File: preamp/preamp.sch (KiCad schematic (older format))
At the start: 37 parts, among them P1 Plug entrada, U1 N35532, U2 N35532

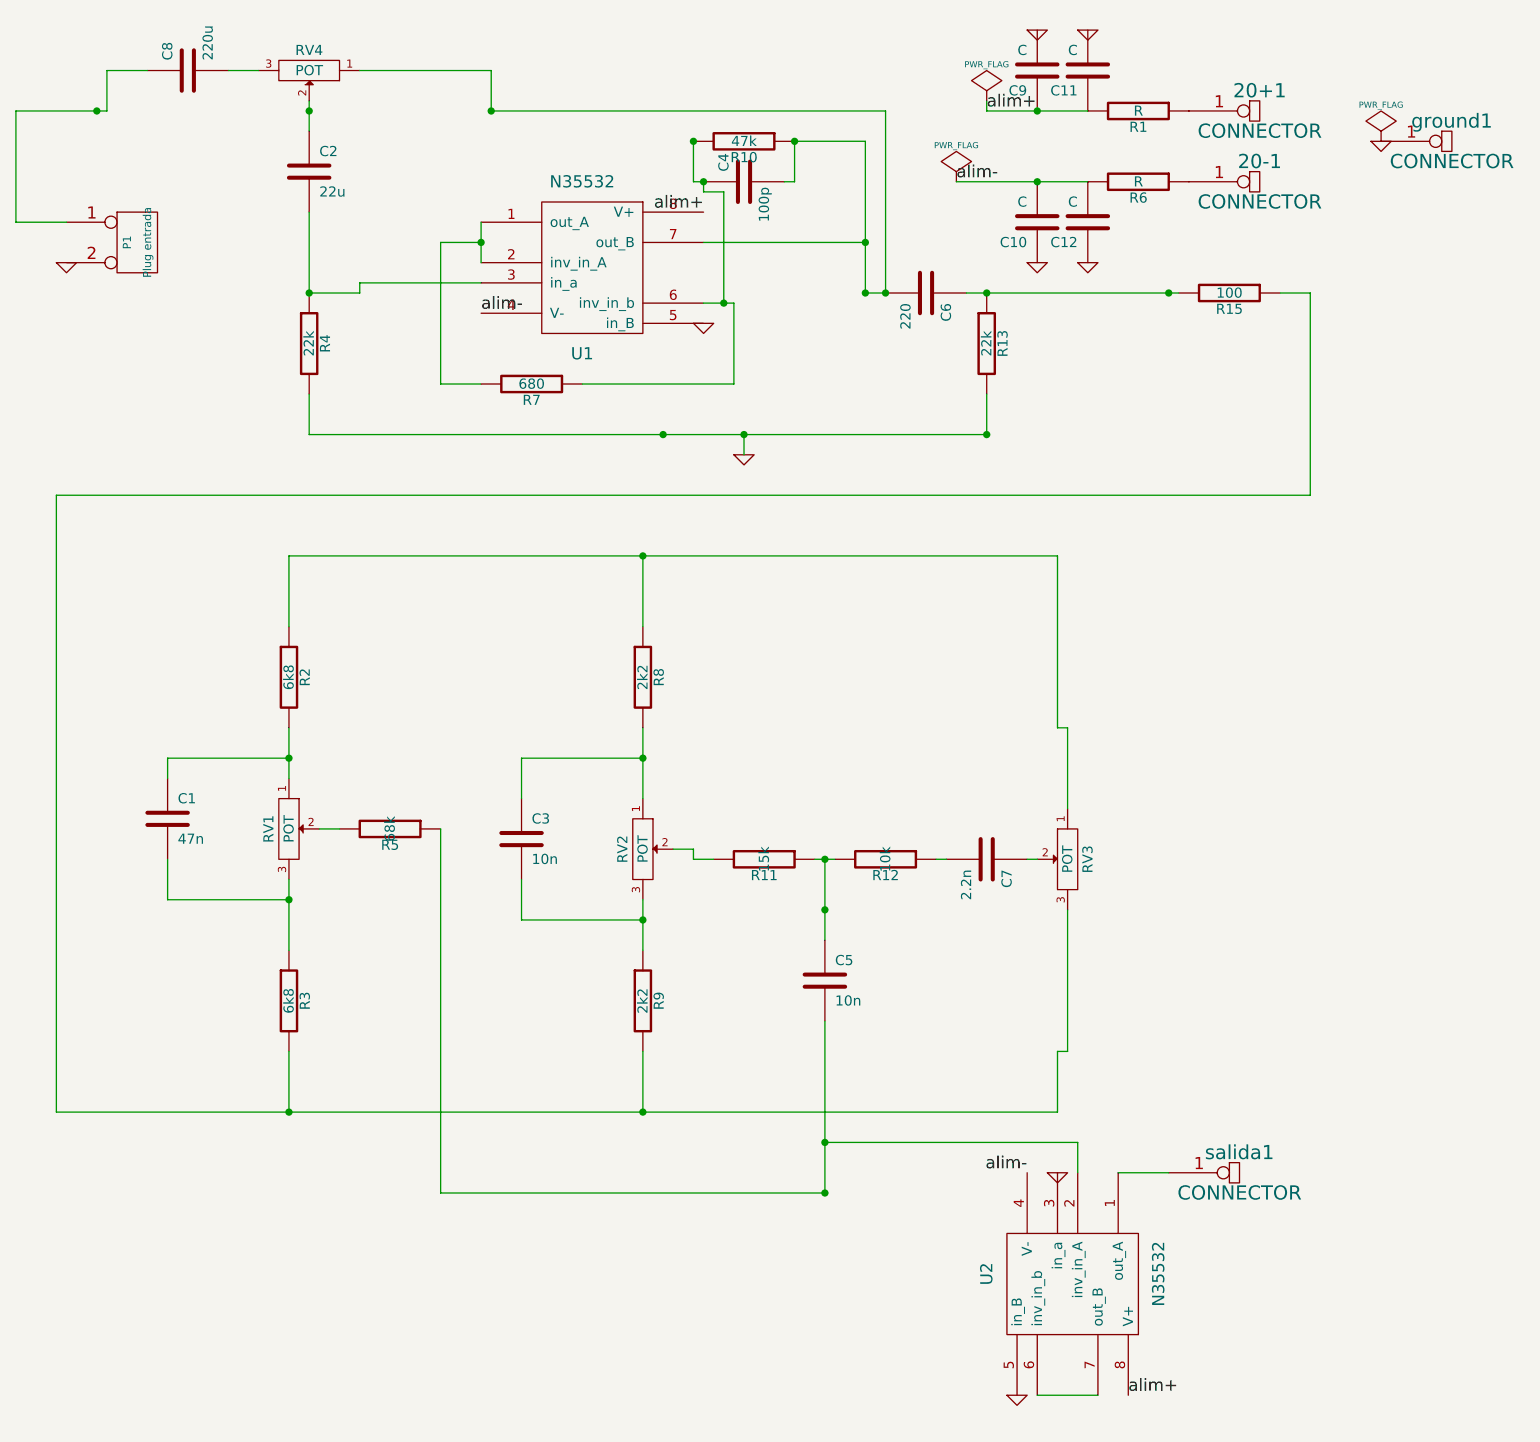
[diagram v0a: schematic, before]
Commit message: 
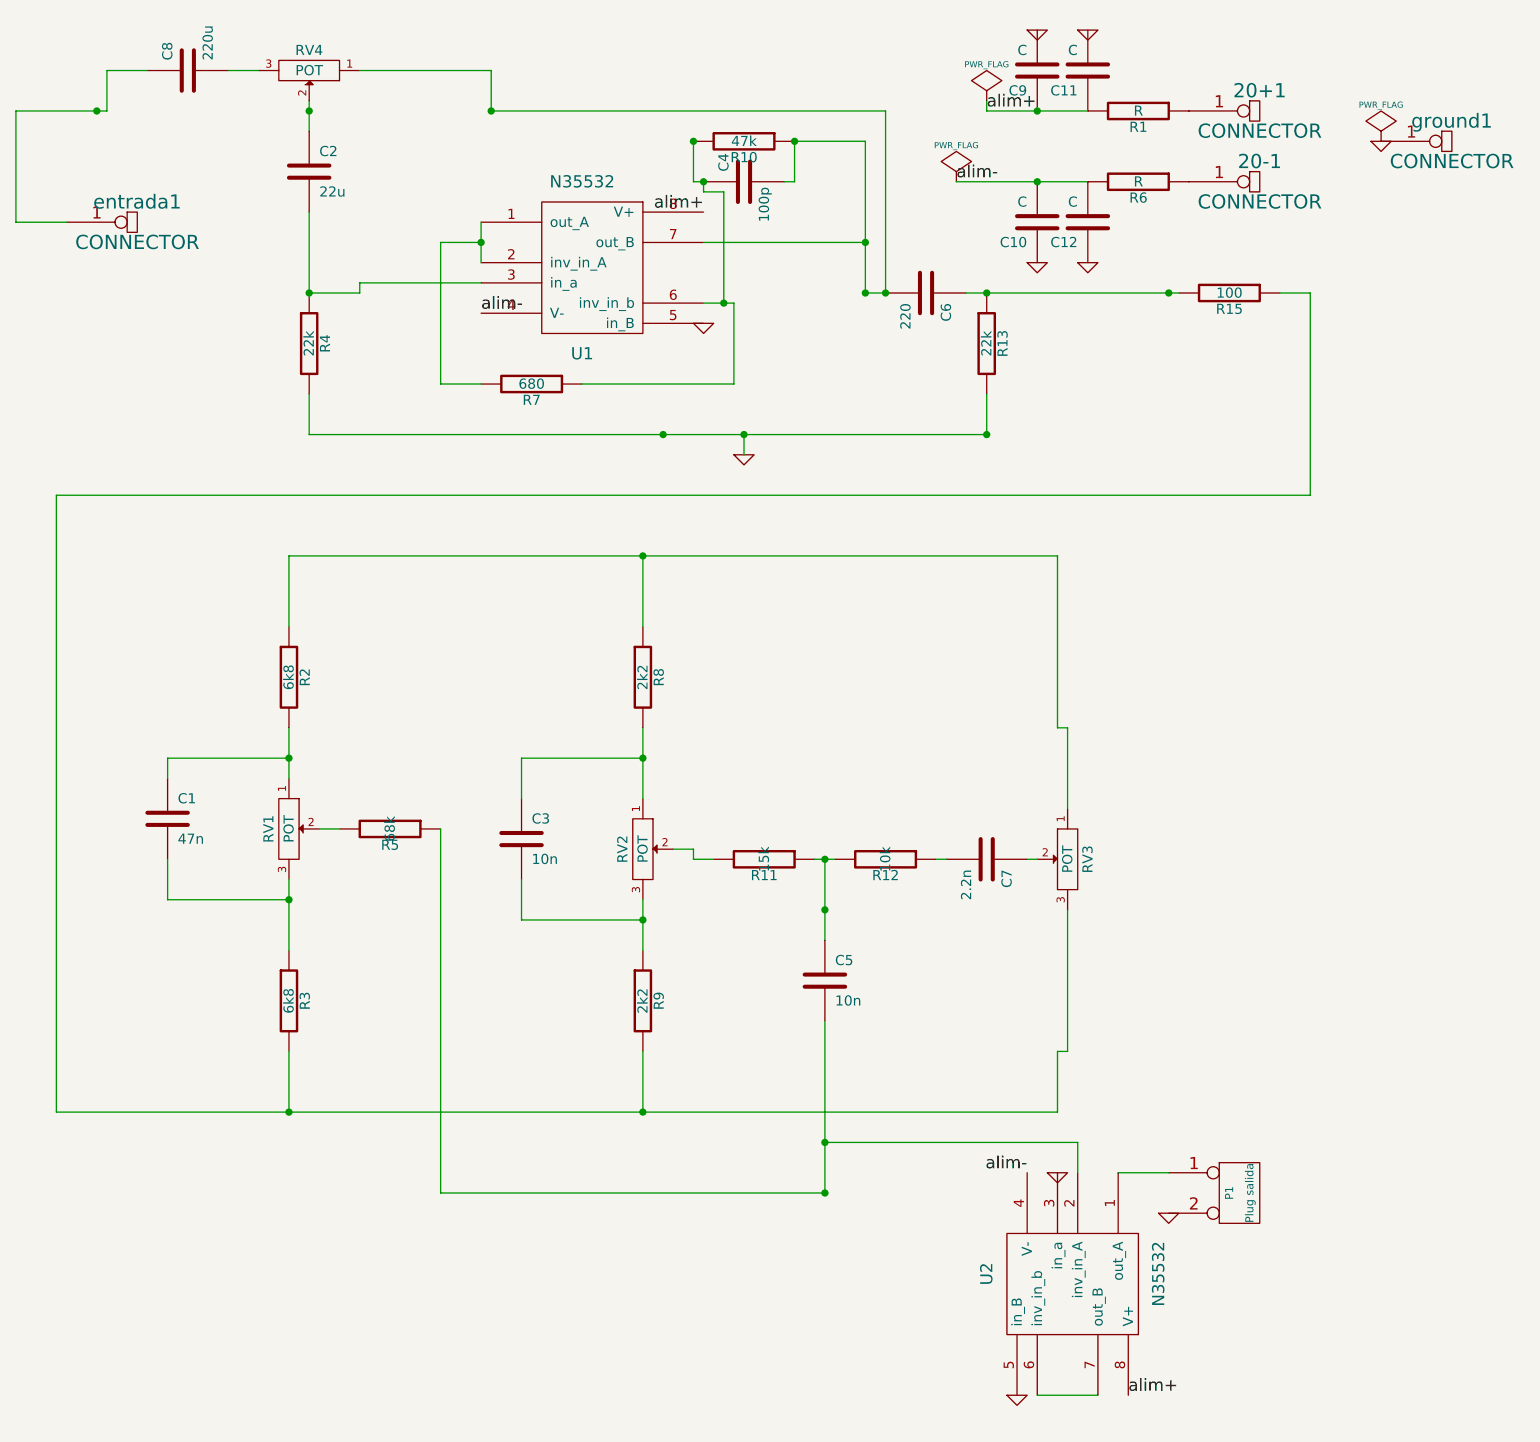
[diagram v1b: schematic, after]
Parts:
- P1: value Plug entrada -> Plug salida
- renumbered salida1 to entrada1
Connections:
- net at entrada1.1 (W): now also C8.1; no longer U2.1 (out_A)
- net at P1.1 (P1): now also U2.1 (out_A); no longer C8.1
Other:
- moved on the sheet: P1, entrada1
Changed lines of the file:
@@
-EESchema Schematic File Version 2  date vie 20 jul 2012 00:23:15 ART
+EESchema Schematic File Version 2  date sáb 21 jul 2012 13:38:50 ART
 LIBS:power
 LIBS:device
@@
 Sheet 1 1
 Title ""
-Date "20 jul 2012"
+Date "21 jul 2012"
 Rev ""
 Comp ""
@@
 L GND #PWR07
 U 1 1 4FF86E92
-P 1750 1550
-F 0 "#PWR07" H 1750 1550 30  0001 C CNN
-F 1 "GND" H 1750 1480 30  0001 C CNN
-	1    1750 1550
+P 7200 6250
+F 0 "#PWR07" H 7200 6250 30  0001 C CNN
+F 1 "GND" H 7200 6180 30  0001 C CNN
+	1    7200 6250
 	1    0    0    -1
 $EndComp
@@
 L CONN_2 P1
 U 1 1 4FF86010
-P 2100 1450
-F 0 "P1" V 2050 1450 40  0000 C CNN
-F 1 "Plug entrada" V 2150 1450 40  0000 C CNN
-	1    2100 1450
+P 7550 6150
+F 0 "P1" V 7500 6150 40  0000 C CNN
+F 1 "Plug salida" V 7600 6150 40  0000 C CNN
+	1    7550 6150
 	1    0    0    -1
 $EndComp
@@
 $EndComp
 $Comp
-L CONNECTOR salida1
+L CONNECTOR entrada1
 U 1 1 4FEE390F
-P 7200 6050
-F 0 "salida1" H 7550 6150 70  0000 C CNN
-F 1 "CONNECTOR" H 7550 5950 70  0000 C CNN
-	1    7200 6050
-	1    0    0    -1
-$EndComp
+P 1750 1350
+F 0 "entrada1" H 2100 1450 70  0000 C CNN
+F 1 "CONNECTOR" H 2100 1250 70  0000 C CNN
+	1    1750 1350
+	1    0    0    -1
+$EndComp

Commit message: 
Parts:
- added ground2: CONNECTOR, symbol CONNECTOR
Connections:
- net GND: now also ground2.1 (W)
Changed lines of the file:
@@
-EESchema Schematic File Version 2  date sáb 21 jul 2012 13:38:50 ART
+EESchema Schematic File Version 2  date sáb 21 jul 2012 23:24:41 ART
 LIBS:power
 LIBS:device
@@
 Sheet 1 1
 Title ""
-Date "21 jul 2012"
+Date "22 jul 2012"
 Rev ""
 Comp ""
@@
 Comment4 ""
 $EndDescr
+$Comp
+L CONNECTOR ground2
+U 1 1 500B641C
+P 6300 2400
+F 0 "ground2" H 6650 2500 70  0000 C CNN
+F 1 "CONNECTOR" H 6650 2300 70  0000 C CNN
+	1    6300 2400
+	1    0    0    -1
+$EndComp
 Wire Wire Line
 	1700 5750 6650 5750

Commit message: algunos cambios actualizados
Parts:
- C6: value 220 -> 220u
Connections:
- net at R2.1, R8.1, RV3.1: now also P1.1 (P1), U2.1 (out_A)
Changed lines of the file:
@@
-EESchema Schematic File Version 2  date sáb 21 jul 2012 23:24:41 ART
+EESchema Schematic File Version 2  date sáb 28 jul 2012 01:18:30 ART
 LIBS:power
 LIBS:device
@@
 Sheet 1 1
 Title ""
-Date "22 jul 2012"
+Date "28 jul 2012"
 Rev ""
 Comp ""
@@
 Comment4 ""
 $EndDescr
+Connection ~ 6700 3900
+Wire Wire Line
+	6700 3900 7150 3900
+Connection ~ 7150 6050
+Wire Wire Line
+	7150 3900 7150 6050
+Connection ~ 6550 800
+Wire Wire Line
+	6300 750  6300 800
+Wire Wire Line
+	6300 800  6800 800
+Connection ~ 6550 1150
+Wire Wire Line
+	6800 1150 6150 1150
+Connection ~ 5700 1450
+Wire Wire Line
+	4900 1450 5700 1450
+Wire Wire Line
+	3800 2150 3600 2150
+Wire Wire Line
+	3600 2150 3600 1450
+Connection ~ 3800 1450
+Wire Wire Line
+	3600 1450 3800 1450
+Wire Wire Line
+	4300 2150 5050 2150
+Wire Wire Line
+	5050 2150 5050 1750
+Wire Wire Line
+	5050 1750 4900 1750
+Wire Wire Line
+	3200 1650 3200 1700
+Wire Wire Line
+	3200 1650 3800 1650
+Wire Wire Line
+	6750 6050 6750 5900
+Connection ~ 5500 5900
+Wire Wire Line
+	6750 5900 5500 5900
+Wire Wire Line
+	2150 600  1950 600
+Wire Wire Line
+	7250 1700 6200 1700
+Wire Wire Line
+	1950 800  1500 800
+Connection ~ 3850 800
+Wire Wire Line
+	3850 600  3850 800
+Wire Wire Line
+	3850 600  3200 600
+Wire Wire Line
+	6550 4500 6500 4500
+Wire Wire Line
+	2850 4950 2850 4600
+Connection ~ 2850 5750
+Wire Wire Line
+	7750 1700 7900 1700
+Connection ~ 5100 2400
+Wire Wire Line
+	5100 2400 5100 2500
+Connection ~ 6300 2400
+Connection ~ 6300 1700
+Wire Wire Line
+	6300 2200 6300 2400
+Wire Wire Line
+	2950 2200 2950 2400
+Wire Wire Line
+	5700 1700 5800 1700
+Wire Wire Line
+	4850 950  4850 1150
+Wire Wire Line
+	4850 1150 4900 1150
+Connection ~ 5500 4750
+Wire Wire Line
+	6700 4250 6700 3850
+Wire Wire Line
+	6700 3850 6650 3850
+Wire Wire Line
+	6650 3850 6650 3000
+Connection ~ 5500 4500
+Wire Wire Line
+	4950 4500 4850 4500
+Wire Wire Line
+	4850 4500 4850 4450
+Wire Wire Line
+	4850 4450 4750 4450
+Connection ~ 4600 5750
+Wire Wire Line
+	4600 5450 4600 5750
+Connection ~ 4600 3000
+Wire Wire Line
+	4600 3350 4600 3000
+Connection ~ 4600 4000
+Wire Wire Line
+	4600 4000 4000 4000
+Wire Wire Line
+	4000 4000 4000 4200
+Wire Wire Line
+	4600 3850 4600 4200
+Connection ~ 2850 4000
+Wire Wire Line
+	2850 4000 2250 4000
+Wire Wire Line
+	2250 4000 2250 4100
+Wire Wire Line
+	2850 4100 2850 3850
+Wire Wire Line
+	2250 4500 2250 4700
+Wire Wire Line
+	2250 4700 2850 4700
+Connection ~ 2850 4700
+Wire Wire Line
+	4600 4950 4600 4700
+Wire Wire Line
+	4000 4600 4000 4800
+Wire Wire Line
+	4000 4800 4600 4800
+Connection ~ 4600 4800
+Wire Wire Line
+	6650 3000 2850 3000
+Wire Wire Line
+	2850 3000 2850 3350
+Wire Wire Line
+	2850 5750 2850 5450
+Wire Wire Line
+	6650 5450 6650 5750
+Wire Wire Line
+	5450 4500 5550 4500
+Wire Wire Line
+	6100 4500 6050 4500
+Wire Wire Line
+	6650 5450 6700 5450
+Wire Wire Line
+	6700 5450 6700 4750
+Wire Wire Line
+	3600 4350 3600 6150
+Wire Wire Line
+	3600 6150 5500 6150
+Connection ~ 5500 6150
+Wire Wire Line
+	3200 1700 2950 1700
+Wire Wire Line
+	5700 950  5350 950
+Wire Wire Line
+	5700 950  5700 1700
+Wire Wire Line
+	5350 950  5350 1150
+Wire Wire Line
+	5350 1150 5300 1150
+Wire Wire Line
+	5800 1700 5800 800
+Connection ~ 4700 2400
+Wire Wire Line
+	2950 1700 2950 1300
+Wire Wire Line
+	6950 6050 7200 6050
+Connection ~ 2950 1700
+Connection ~ 2950 800
+Connection ~ 4850 950
+Connection ~ 5350 950
+Connection ~ 5800 1700
+Connection ~ 5700 1700
+Connection ~ 7200 1700
+Wire Wire Line
+	3000 4350 3100 4350
+Wire Wire Line
+	5500 4900 5500 4500
+Connection ~ 1900 800
+Wire Wire Line
+	1950 800  1950 600
+Wire Wire Line
+	2950 900  2950 750
+Wire Wire Line
+	5800 800  3850 800
+Wire Wire Line
+	2950 2400 6300 2400
+Wire Wire Line
+	2700 600  2550 600
+Wire Wire Line
+	1500 800  1500 1350
+Wire Wire Line
+	1500 1350 1750 1350
+Wire Wire Line
+	6550 7150 6850 7150
+Wire Wire Line
+	5500 6150 5500 5300
+Wire Wire Line
+	3800 1550 3800 1350
+Wire Wire Line
+	4900 1150 4900 1200
+Wire Wire Line
+	4900 1200 5000 1200
+Wire Wire Line
+	5000 1200 5000 1750
+Connection ~ 5000 1750
+Connection ~ 4900 1150
+Wire Wire Line
+	7900 1700 7900 2700
+Wire Wire Line
+	7900 2700 1700 2700
+Wire Wire Line
+	1700 2700 1700 5750
+Wire Wire Line
+	1700 5750 6650 5750
 $Comp
 L CONNECTOR ground2
@@
 	1    0    0    -1
 $EndComp
-Wire Wire Line
-	1700 5750 6650 5750
-Wire Wire Line
-	1700 5750 1700 2700
-Wire Wire Line
-	1700 2700 7900 2700
-Wire Wire Line
-	7900 2700 7900 1700
-Connection ~ 4900 1150
-Connection ~ 5000 1750
-Wire Wire Line
-	5000 1750 5000 1200
-Wire Wire Line
-	5000 1200 4900 1200
-Wire Wire Line
-	4900 1200 4900 1150
-Wire Wire Line
-	3800 1550 3800 1350
-Wire Wire Line
-	5500 5300 5500 6150
-Wire Wire Line
-	6550 7150 6850 7150
-Wire Wire Line
-	1750 1350 1500 1350
-Wire Wire Line
-	1500 1350 1500 800
-Wire Wire Line
-	2700 600  2550 600
-Wire Wire Line
-	2950 2400 6300 2400
-Wire Wire Line
-	5800 800  3850 800
-Wire Wire Line
-	2950 900  2950 750
-Wire Wire Line
-	1950 800  1950 600
-Connection ~ 1900 800
-Wire Wire Line
-	5500 4900 5500 4500
-Wire Wire Line
-	3000 4350 3100 4350
-Connection ~ 7200 1700
-Connection ~ 5700 1700
-Connection ~ 5800 1700
-Connection ~ 5350 950
-Connection ~ 4850 950
-Connection ~ 2950 800
-Connection ~ 2950 1700
-Wire Wire Line
-	6950 6050 7200 6050
-Wire Wire Line
-	2950 1300 2950 1700
-Connection ~ 4700 2400
-Wire Wire Line
-	5800 800  5800 1700
-Wire Wire Line
-	5300 1150 5350 1150
-Wire Wire Line
-	5350 1150 5350 950
-Wire Wire Line
-	5700 950  5700 1700
-Wire Wire Line
-	5700 950  5350 950
-Wire Wire Line
-	2950 1700 3200 1700
-Connection ~ 5500 6150
-Wire Wire Line
-	5500 6150 3600 6150
-Wire Wire Line
-	3600 6150 3600 4350
-Wire Wire Line
-	6700 4750 6700 5450
-Wire Wire Line
-	6700 5450 6650 5450
-Wire Wire Line
-	6100 4500 6050 4500
-Wire Wire Line
-	5450 4500 5550 4500
-Wire Wire Line
-	6650 5450 6650 5750
-Wire Wire Line
-	2850 5750 2850 5450
-Wire Wire Line
-	2850 3350 2850 3000
-Wire Wire Line
-	2850 3000 6650 3000
-Connection ~ 4600 4800
-Wire Wire Line
-	4600 4800 4000 4800
-Wire Wire Line
-	4000 4800 4000 4600
-Wire Wire Line
-	4600 4950 4600 4700
-Connection ~ 2850 4700
-Wire Wire Line
-	2850 4700 2250 4700
-Wire Wire Line
-	2250 4700 2250 4500
-Wire Wire Line
-	2850 4100 2850 3850
-Wire Wire Line
-	2250 4100 2250 4000
-Wire Wire Line
-	2250 4000 2850 4000
-Connection ~ 2850 4000
-Wire Wire Line
-	4600 3850 4600 4200
-Wire Wire Line
-	4000 4200 4000 4000
-Wire Wire Line
-	4000 4000 4600 4000
-Connection ~ 4600 4000
-Wire Wire Line
-	4600 3350 4600 3000
-Connection ~ 4600 3000
-Wire Wire Line
-	4600 5450 4600 5750
-Connection ~ 4600 5750
-Wire Wire Line
-	4750 4450 4850 4450
-Wire Wire Line
-	4850 4450 4850 4500
-Wire Wire Line
-	4850 4500 4950 4500
-Connection ~ 5500 4500
-Wire Wire Line
-	6650 3000 6650 3850
-Wire Wire Line
-	6650 3850 6700 3850
-Wire Wire Line
-	6700 3850 6700 4250
-Connection ~ 5500 4750
-Wire Wire Line
-	4900 1150 4850 1150
-Wire Wire Line
-	4850 1150 4850 950
-Wire Wire Line
-	5700 1700 5800 1700
-Wire Wire Line
-	2950 2400 2950 2200
-Wire Wire Line
-	6300 2400 6300 2200
-Connection ~ 6300 1700
-Connection ~ 6300 2400
-Wire Wire Line
-	5100 2400 5100 2500
-Connection ~ 5100 2400
-Wire Wire Line
-	7900 1700 7750 1700
-Connection ~ 2850 5750
-Wire Wire Line
-	2850 4950 2850 4600
-Wire Wire Line
-	6550 4500 6500 4500
-Wire Wire Line
-	3200 600  3850 600
-Wire Wire Line
-	3850 600  3850 800
-Connection ~ 3850 800
-Wire Wire Line
-	1950 800  1500 800
-Wire Wire Line
-	7250 1700 6200 1700
-Wire Wire Line
-	1950 600  2150 600
-Wire Wire Line
-	5500 5900 6750 5900
-Connection ~ 5500 5900
-Wire Wire Line
-	6750 5900 6750 6050
-Wire Wire Line
-	3800 1650 3200 1650
-Wire Wire Line
-	3200 1650 3200 1700
-Wire Wire Line
-	4900 1750 5050 1750
-Wire Wire Line
-	5050 1750 5050 2150
-Wire Wire Line
-	5050 2150 4300 2150
-Wire Wire Line
-	3800 1450 3600 1450
-Connection ~ 3800 1450
-Wire Wire Line
-	3600 1450 3600 2150
-Wire Wire Line
-	3600 2150 3800 2150
-Wire Wire Line
-	4900 1450 5700 1450
-Connection ~ 5700 1450
-Wire Wire Line
-	6800 1150 6150 1150
-Connection ~ 6550 1150
-Wire Wire Line
-	6800 800  6300 800
-Wire Wire Line
-	6300 800  6300 750
-Connection ~ 6550 800
 $Comp
 L N35532 U2
@@
 P 6000 1700
 F 0 "C6" H 6050 1800 50  0000 L CNN
-F 1 "220" H 6050 1600 50  0000 L CNN
+F 1 "220u" H 6050 1600 50  0000 L CNN
 	1    6000 1700
 	0    1    1    0
